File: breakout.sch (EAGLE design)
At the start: 3 parts, among them X1 SCART-F

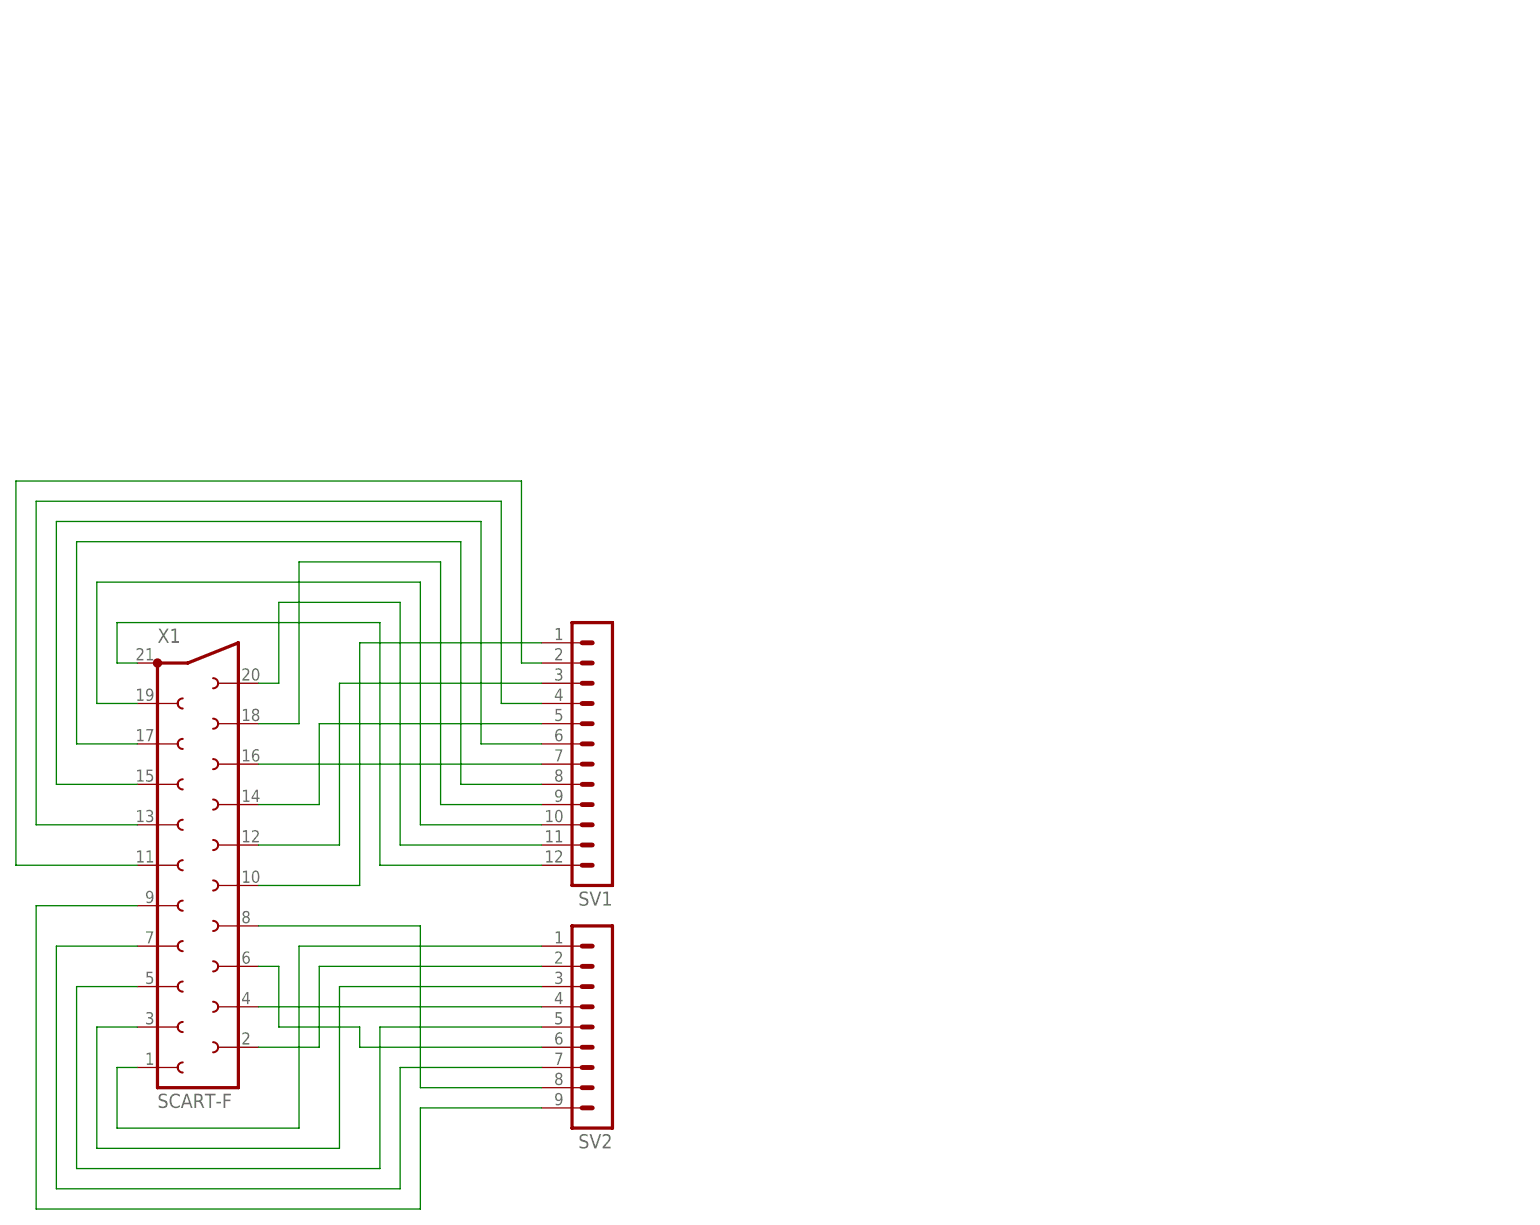
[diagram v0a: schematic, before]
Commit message: Version 2 of the breakout board
- Created a 21-pin header part instead of using 9 & 12-pin parts
- Routed all the wires manually on the bottom layer
- Added the pinouts as documented on Wikipedia to the top layer at the
  expense of making the board slightly bigger
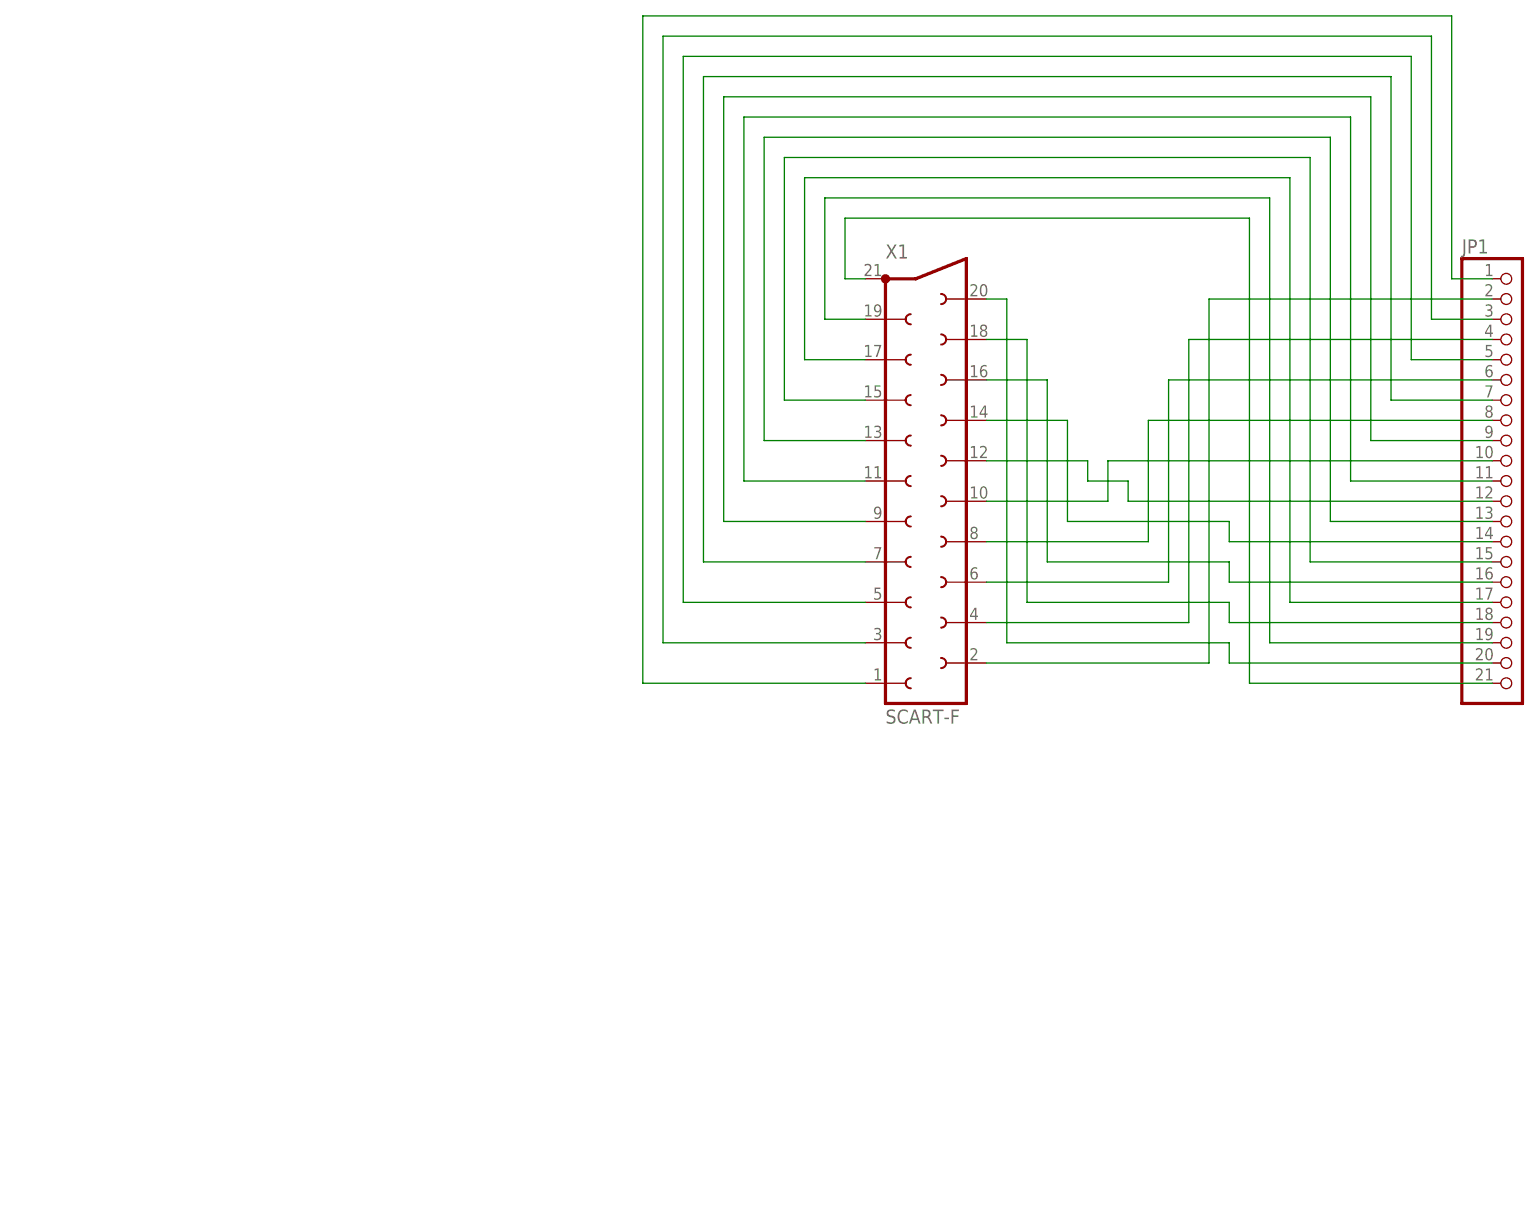
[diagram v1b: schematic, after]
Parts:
- removed SV1: (no value), con-lstb:MA12-1
- removed SV2: (no value), con-lstb:MA09-1
- added JP1: (no value), pinhead:PINHD-1X21
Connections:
- net N$1: now also JP1.10, X1.10; no longer SV2.1, X1.1
- net N$10: now also JP1.20, X1.20; no longer SV1.1, X1.10
- net N$11: now also JP1.21, X1.21; no longer SV1.2, X1.11
- net N$12: now also JP1.19, X1.19; no longer SV1.3, X1.12
- net N$13: now also JP1.17, X1.17; no longer SV1.4, X1.13
- net N$14: now also JP1.15, X1.15; no longer SV1.5, X1.14
- net N$15: now also JP1.13, X1.13; no longer SV1.6, X1.15
- net N$16: now also JP1.11, X1.11; no longer SV1.7, X1.16
- net N$17: now also JP1.9, X1.9; no longer SV1.8, X1.17
- net N$18: now also JP1.7, X1.7; no longer SV1.9, X1.18
- net N$19: now also JP1.5, X1.5; no longer SV1.10, X1.19
- net N$2: now also JP1.12, X1.12; no longer SV2.2, X1.2
- net N$20: now also JP1.3, X1.3; no longer SV1.11, X1.20
- net N$21: now also JP1.1, X1.1; no longer SV1.12, X1.21
- net N$3: now also JP1.8, X1.8; no longer SV2.3, X1.3
- net N$4: now also JP1.6, X1.6; no longer SV2.4, X1.4
- net N$5: now also JP1.4, X1.4; no longer SV2.5, X1.5
- net N$6: now also JP1.2, X1.2; no longer SV2.6, X1.6
- net N$7: now also JP1.14, X1.14; no longer SV2.7, X1.7
- net N$8: now also JP1.16, X1.16; no longer SV2.8, X1.8
- net N$9: now also JP1.18, X1.18; no longer SV2.9, X1.9
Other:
- moved on the sheet: X1
